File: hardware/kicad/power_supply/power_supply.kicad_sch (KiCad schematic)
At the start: 30 parts, among them J1 USB_C_Receptacle_PowerOnly_6P, J2 PINHD_1x4_Female, Q1 AO3401A, U1 TP4056-42-ESOP8, U2 MT3608

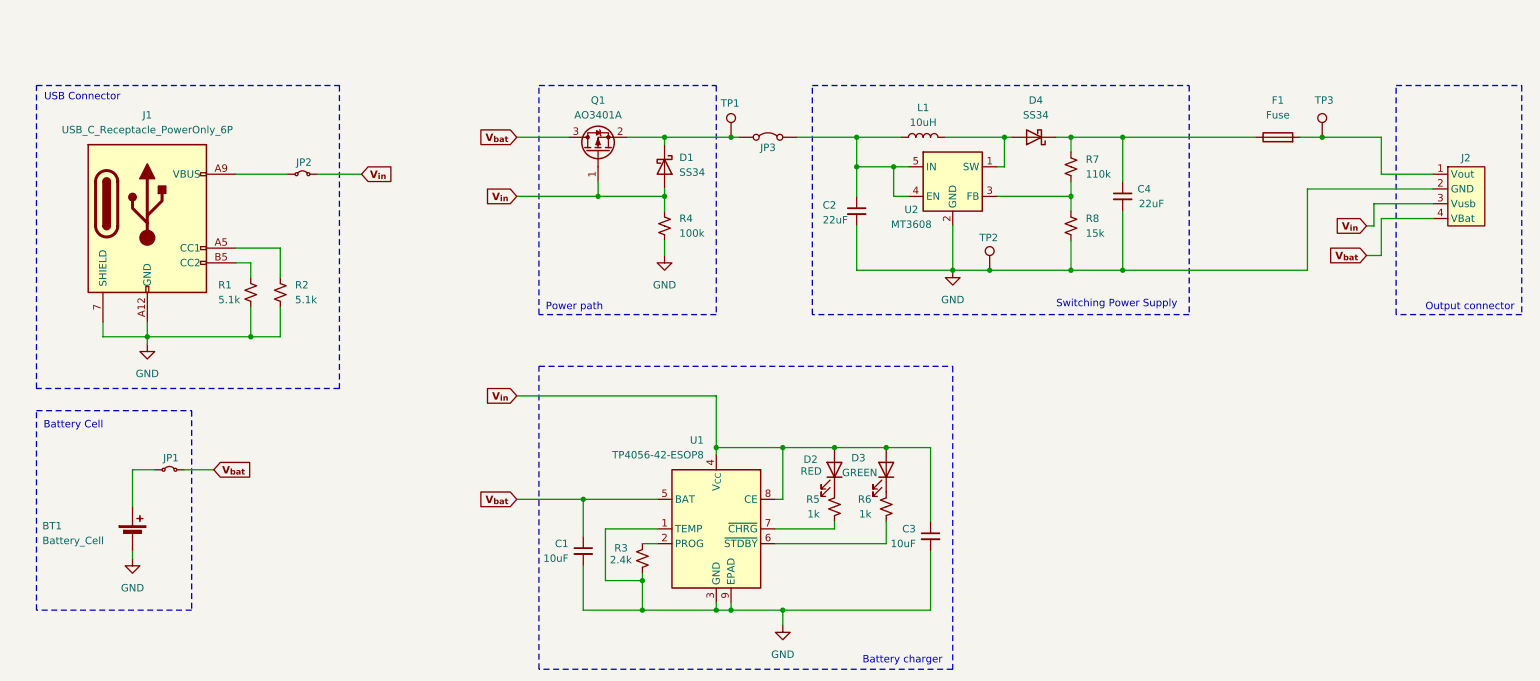
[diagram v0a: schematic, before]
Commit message: Visual changes on KiCAD projects
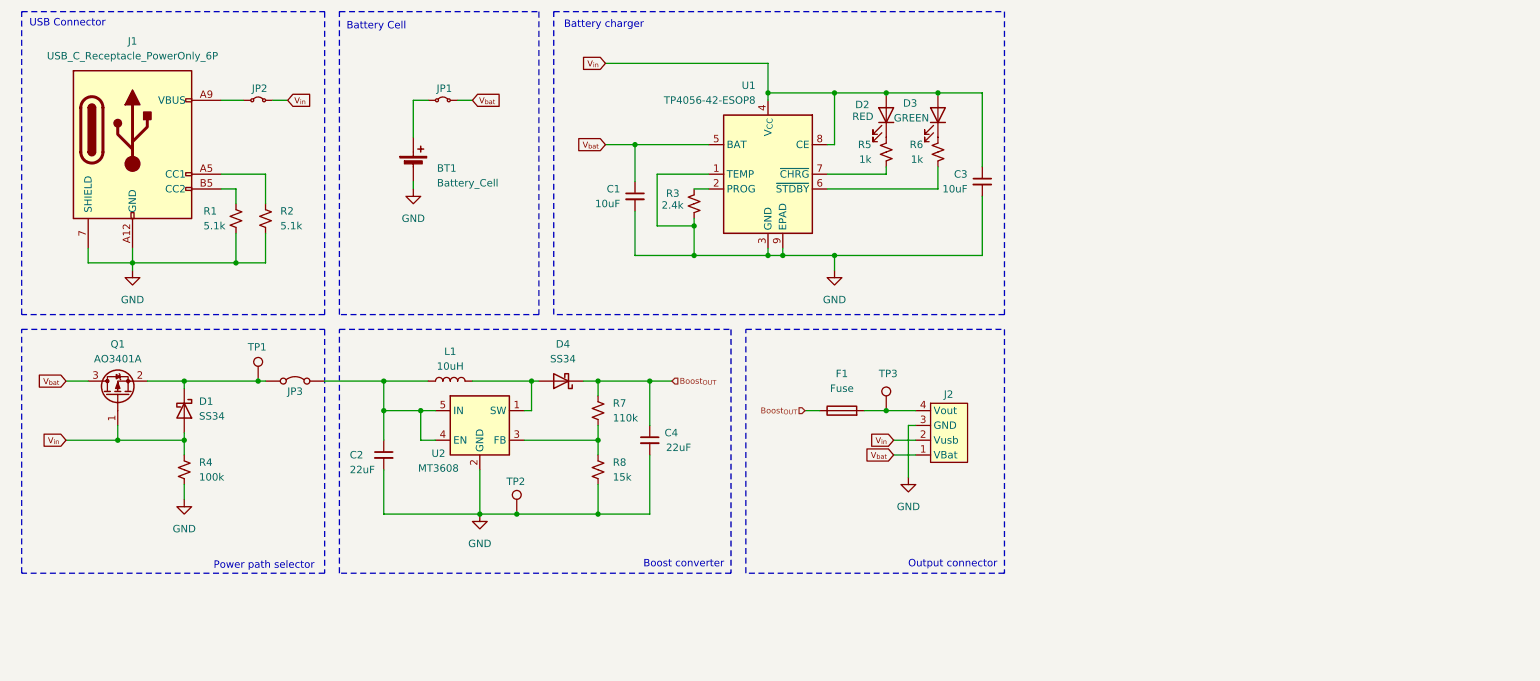
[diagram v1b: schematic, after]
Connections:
- net GND: now also J2.3 (GND); no longer J2.2 (GND)
- net V_{bat}: now also J2.1 (VBat); no longer J2.4 (VBat)
- net V_{in}: now also J2.2 (Vusb); no longer J2.3 (Vusb)
- net Boost_{OUT}: now reaches C4.1, D4.1 (K), F1.1, R7.1
- net at F1.2, TP3.1: now also J2.4 (Vout); no longer J2.1 (Vout)
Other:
- note added: "Boost converter"
- note added: "Power path selector"
- note removed: "Power path"
- note removed: "Switching Power Supply"
- moved on the sheet: BT1, C1, C2, C3, C4, D1, D2, D3, D4, F1, J1, J2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
